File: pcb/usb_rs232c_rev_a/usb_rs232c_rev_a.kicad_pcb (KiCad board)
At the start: 2 copper layers, 35.1 x 14.4 mm, 29 parts, among them J1 USB_A, J2 RS-232, U1 CH340G, U2 MAX232, Y1 12MHz

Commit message: Updated PCB after the first iteration.
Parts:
- MH1, MH2: value 1.3mm -> 1.4mm; footprint usb_rs232_footprints:MountingHole_1.3mm -> usb_rs232_footprints:MountingHole_1.4mm
- TP1, TP2: footprint Measurement_Points:Measurement_Point_Round-SMD-Pad_Small -> usb_rs232_footprints:Measurement_Point_Square-SMD_1.0mmx1.0mm
- moved C10 1.71 mm to (120.3, 92.5)
- moved C6 0.89 mm to (122.0, 94.6)
- moved MH1 0.05 mm to (109.1, 87.3)
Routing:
- net GNDREF: track 9.34 -> 10.6 mm, vias 5 -> 6
- net /C1+: track 1.93 -> 2.82 mm
- net /C1-: track 3.34 -> 2.58 mm
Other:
- board size 35.1 x 14.4 mm -> 34.7 x 14.4 mm

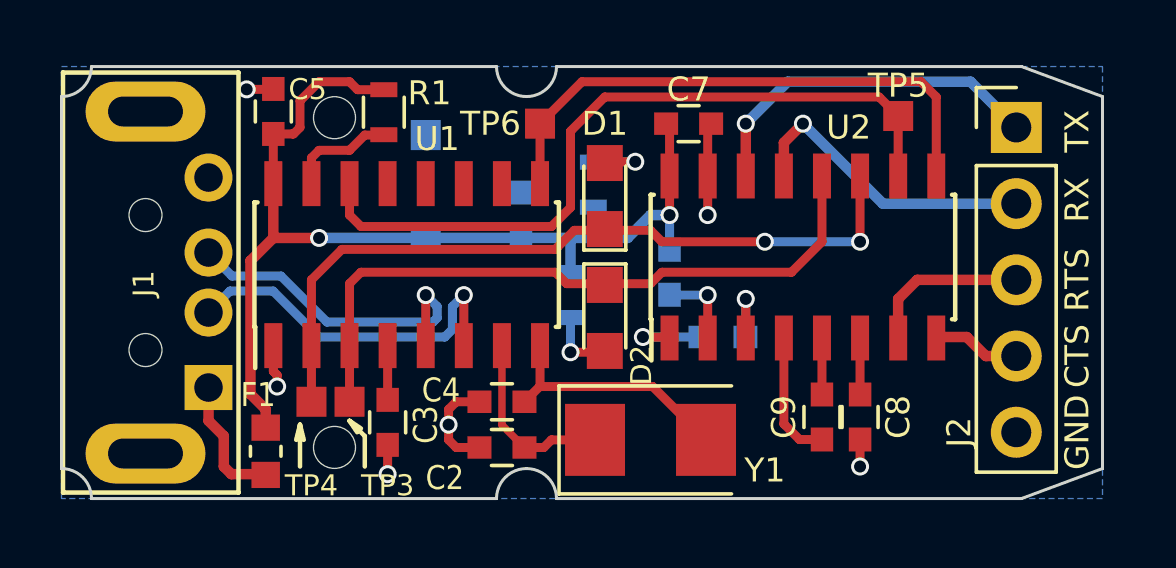
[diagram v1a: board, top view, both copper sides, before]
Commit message: 1. Added bypass resistors for MAX232. 2. Updated README.md
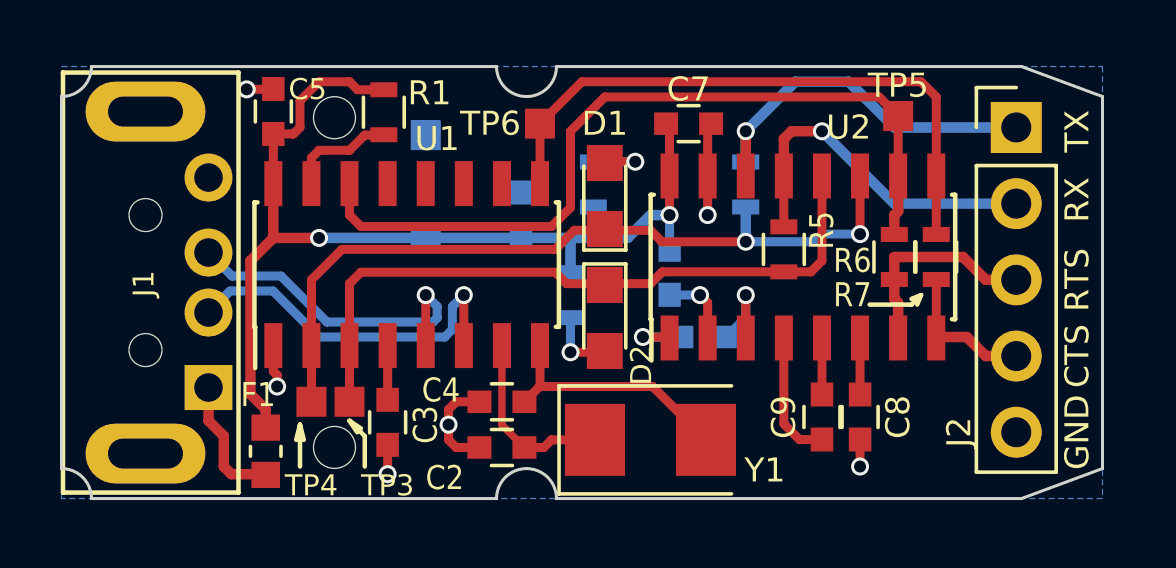
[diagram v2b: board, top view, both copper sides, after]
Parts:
- added R4: 0, Resistors_SMD:R_0603, B.Cu at (122.8, 89.5)
- added R5: 0, Resistors_SMD:R_0603, F.Cu at (124.1, 91.7)
- added R6: 0, Resistors_SMD:R_0603, F.Cu at (127.8, 91.9)
- added R7: 0, Resistors_SMD:R_0603, F.Cu at (129.2, 91.9)
- moved C6 0.63 mm to (121.4, 94.6)
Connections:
- U1 pad 10: Net-(U1-Pad10) -> (no net)
- U1 pad 11: Net-(U1-Pad11) -> (no net)
- U1 pad 12: Net-(U1-Pad12) -> (no net)
- U1 pad 13: Net-(U1-Pad13) -> (no net)
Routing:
- net /RTS#: track 25.0 -> 27.0 mm
- net /CTS: track 3.07 -> 5.02 mm
- net /CTS#: track 18.6 -> 20.6 mm
- net /RTS: track 5.63 -> 7.13 mm
- net /RX: track 10.4 -> 11.8 mm
- net /TXD: track 25.4 -> 26.4 mm
- net /TX: track 12.0 -> 12.9 mm
- net /C1+: track 2.82 -> 2.18 mm
- net /C1-: track 2.58 -> 3.11 mm

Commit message: Schematics update.
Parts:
- C10, C6, C8, C9: value 10uF -> 1uF
- C3: value 10uF -> 10nF
- C5: value 10uF -> 100nF
- J2: value RS-232 -> RS-232/UART
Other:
- board text added: "RS-232/UART"
- board text removed: "RS-232"
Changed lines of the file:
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@@
     (links 62)
     (no_connects 0)
-    (area 90.021429 71.9 142.428573 102.075)
+    (area 99.949999 85.549999 134.750001 100.050001)
     (thickness 1.6)
     (drawings 39)
@@
   )
   (setup
-    (last_trace_width 0.35)
+    (last_trace_width 0.25)
     (user_trace_width 0.3)
     (user_trace_width 0.35)
@@
       (effects (font (size 0.8 0.8) (thickness 0.1)))
     )
-    (fp_text value RS-232 (at -0.381 12.7) (layer F.Fab)
+    (fp_text value RS-232/UART (at -0.381 12.7) (layer F.Fab)
       (effects (font (size 0.5 0.5) (thickness 0.05)))
     )
@@
       (effects (font (size 0.8 0.7) (thickness 0.1)))
     )
-    (fp_text value 10uF (at 0.0508 0 90) (layer F.Fab)
+    (fp_text value 10nF (at 0.0508 0 90) (layer F.Fab)
       (effects (font (size 0.5 0.5) (thickness 0.05)))
     )
@@
       (effects (font (size 0.7 0.7) (thickness 0.1)))
     )
-    (fp_text value 10uF (at -0.0254 0 90) (layer F.Fab)
+    (fp_text value 100nF (at -0.0254 0 90) (layer F.Fab)
       (effects (font (size 0.5 0.5) (thickness 0.05)))
     )
@@
       (effects (font (size 0.8 0.8) (thickness 0.1)) (justify mirror))
     )
-    (fp_text value 10uF (at 0 0) (layer B.Fab)
+    (fp_text value 1uF (at 0 0) (layer B.Fab)
       (effects (font (size 0.5 0.5) (thickness 0.05)) (justify mirror))
     )
@@
       (effects (font (size 0.8 0.8) (thickness 0.1)))
     )
-    (fp_text value 10uF (at 0 0 90) (layer F.Fab)
+    (fp_text value 1uF (at 0 0 90) (layer F.Fab)
       (effects (font (size 0.5 0.5) (thickness 0.05)))
     )
@@
       (effects (font (size 0.8 0.8) (thickness 0.1)))
     )
-    (fp_text value 10uF (at 0 0 90) (layer F.Fab)
+    (fp_text value 1uF (at 0 0 90) (layer F.Fab)
       (effects (font (size 0.5 0.5) (thickness 0.05)))
     )
@@
       (effects (font (size 0.8 0.8) (thickness 0.1)) (justify mirror))
     )
-    (fp_text value 10uF (at 0 0 270) (layer B.Fab)
+    (fp_text value 1uF (at 0 0 270) (layer B.Fab)
       (effects (font (size 0.5 0.5) (thickness 0.1)) (justify mirror))
     )
@@
   (gr_line (start 110.109 97.917) (end 109.601 97.409) (angle 90) (layer F.SilkS) (width 0.15))
   (gr_line (start 134.7 86.6) (end 134.7 99) (angle 90) (layer Edge.Cuts) (width 0.1))
-  (gr_text RS-232 (at 133.731 92.71 90) (layer B.SilkS)
+  (gr_text RS-232/UART (at 133.731 92.71 90) (layer B.SilkS)
     (effects (font (size 1 1) (thickness 0.2)) (justify mirror))
   )
